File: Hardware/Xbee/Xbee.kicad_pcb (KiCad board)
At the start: 2 copper layers, 100 x 50 mm, 41 parts, among them J1 Alimentación, J2 Raspberry, J3 Pines 1, J4 Pines 2, J5 Programación, J6 Entrada, J7 Salida, J8 Batería, K1 SANYOU_SRD_Form_C, Q1 2N7002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

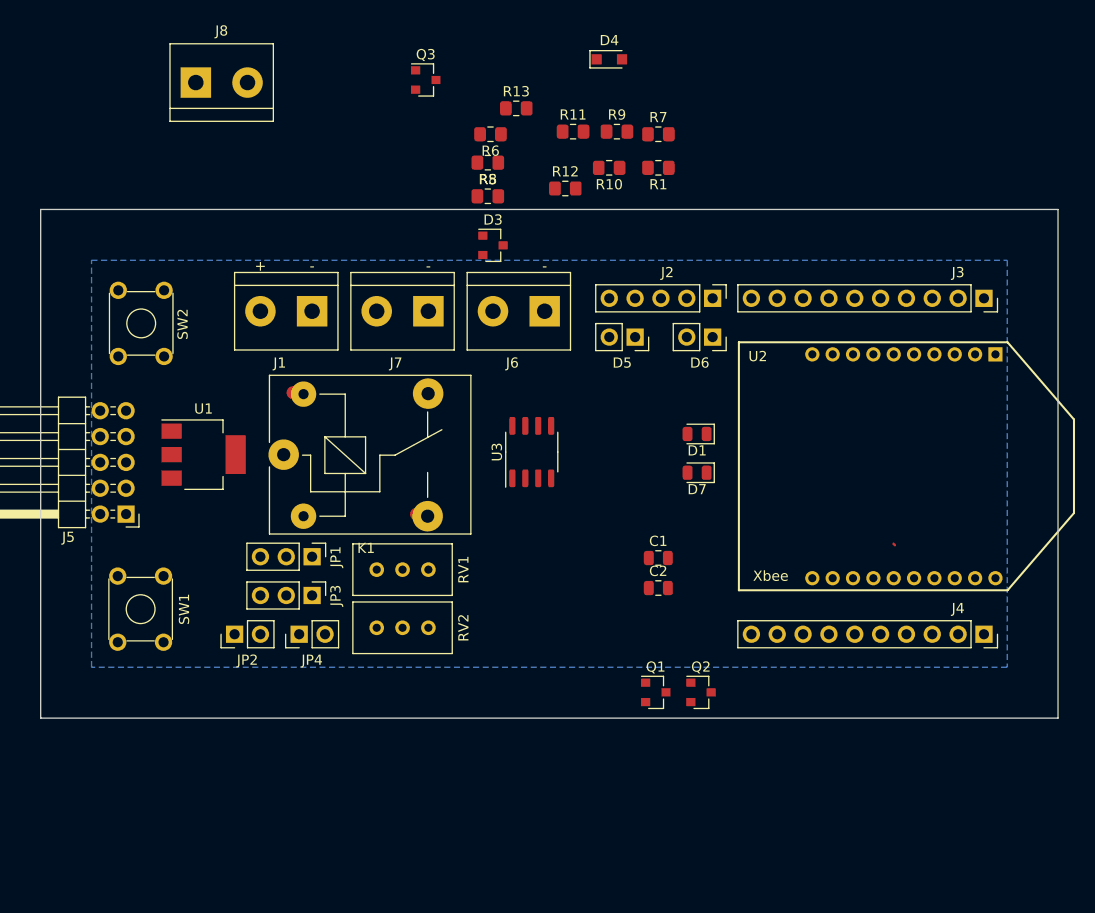
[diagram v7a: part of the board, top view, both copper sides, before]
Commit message: PCB Component Placement
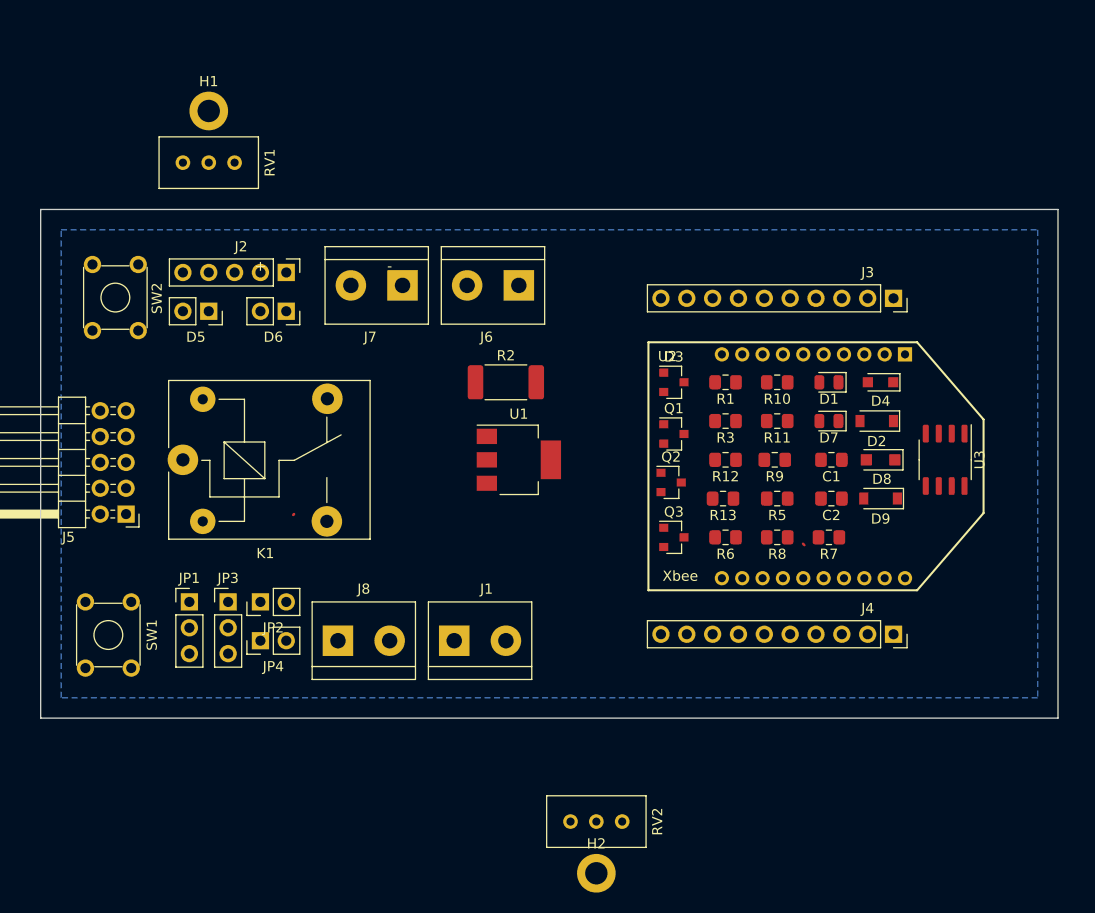
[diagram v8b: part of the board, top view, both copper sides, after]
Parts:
- added D2: DSU24, Diode_SMD:D_SOD-123, F.Cu at (162.2, 50.8)
- added D8: DSK26, Diode_SMD:D_SOD-123F, F.Cu at (162.6, 54.6)
- added D9: DSU24, Diode_SMD:D_SOD-123, F.Cu at (162.6, 58.4)
- added H1: PoteCarga, MountingHole:MountingHole_2.2mm_M2_DIN965_Pad, F.Cu at (96.5, 20.3)
- added H2: PoteEstado, MountingHole:MountingHole_2.2mm_M2_DIN965_Pad, F.Cu at (134.6, 95.2)
- added R2: 100, Resistor_SMD:R_2512_6332Metric_Pad1.52x3.35mm_HandSolder, F.Cu at (125.7, 47.0)
- added R3: 10k, Resistor_SMD:R_0805_2012Metric_Pad1.15x1.40mm_HandSolder, F.Cu at (147.3, 50.8)
- C1, C2: footprint Capacitor_SMD:C_0805_2012Metric -> Capacitor_SMD:C_0805_2012Metric_Pad1.15x1.40mm_HandSolder
- D4: value 1N4007WS -> DSK26
- Q3: value DMP3013SFV -> DMP3099L-7
- moved J8 56.6 mm to (109.2, 72.4)
- moved Q3 51.1 mm to (142.2, 62.2)
- moved R6 45.9 mm to (147.3, 62.2)
- moved RV1 44.3 mm to (99.1, 25.4)
- moved R8 44.0 mm to (152.4, 62.2), turned to 180 degrees
- moved R5 43.6 mm to (152.4, 58.4)
- moved R13 43.4 mm to (147.1, 58.4), turned to 180 degrees
- moved R7 43.0 mm to (157.5, 62.2), turned to 180 degrees
- moved D5 42.0 mm to (96.5, 40.0)
- moved D6 42.0 mm to (104.1, 40.0)
- moved J2 42.0 mm to (104.1, 36.2)
- moved D4 41.5 mm to (162.6, 47.0), turned to 180 degrees
- moved U3 40.6 mm to (168.9, 54.6), turned to 270 degrees
- moved R9 35.8 mm to (152.2, 54.6), turned to 180 degrees
- moved J1 35.3 mm to (120.7, 72.4), turned to 0 degrees
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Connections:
- Q3 pad 1: /Vin+ -> /CargaBatería
- Q3 pad 3: /Vin+ -> Net-(D2-Pad2)
- R7 pad 2: +12V -> /Bat+
- RV1 pad 1: +12V -> /Bat+
- RV2 pad 1: +12V -> /Bat+
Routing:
- net +12V: track 1.68 -> 0.00 mm
